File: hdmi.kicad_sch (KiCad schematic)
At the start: 0 parts

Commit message: SCH: Update title block, set revision to 1.0.0
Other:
- company: (none) -> Antmicro Ltd
- title: (none) -> Jetson Orin Baseboard
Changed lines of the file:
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@@
 (kicad_sch (version 20211123) (generator eeschema)
   (paper "A4")
+  (title_block
+    (title "Jetson Orin Baseboard")
+    (rev "1.0.0")
+    (company "Antmicro Ltd")
+    (comment 1 "www.antmicro.com")
+  )
 )

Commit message: Add HDMI connector
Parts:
- added J2: 46756-1001, antmicro-footprints:HDMI_Micro-D_Molex_46765-1x01, symbol antmicroUSBDVIHDMIConnectors:46756-1001
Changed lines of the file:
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@@
     (comment 1 "www.antmicro.com")
   )
+  (symbol (lib_id "antmicroUSBDVIHDMIConnectors:46756-1001") (at 217.17 74.295 0) (unit 1)
+    (in_bom yes) (on_board yes) (fields_autoplaced)
+    (property "Reference" "J2" (id 0) (at 228.092 73.4603 0)
+      (effects (font (size 1.27 1.27)) (justify left))
+    )
+    (property "Value" "46756-1001" (id 1) (at 228.092 75.9972 0)
+      (effects (font (size 1.27 1.27)) (justify left))
+    )
+    (property "Footprint" "antmicro-footprints:HDMI_Micro-D_Molex_46765-1x01" (id 2) (at 217.17 102.235 0)
+      (effects (font (size 1.27 1.27)) hide)
+    )
+    (property "Datasheet" "https://www.molex.com/webdocs/datasheets/pdf/en-us/0467651001_IO_CONNECTORS.pdf" (id 3) (at 217.17 74.295 0)
+      (effects (font (size 1.27 1.27)) hide)
+    )
+    (property "MPN" "467651001" (id 4) (at 217.17 104.775 0)
+      (effects (font (size 1.27 1.27)) hide)
+    )
+    (property "Manufacturer" "Molex" (id 5) (at 217.17 107.315 0)
+      (effects (font (size 1.27 1.27)) hide)
+    )
+    (pin "1")
+    (pin "10")
+    (pin "11")
+    (pin "12")
+    (pin "13")
+    (pin "14")
+    (pin "15")
+    (pin "16")
+    (pin "17")
+    (pin "18")
+    (pin "19")
+    (pin "2")
+    (pin "3")
+    (pin "4")
+    (pin "5")
+    (pin "6")
+    (pin "7")
+    (pin "8")
+    (pin "9")
+    (pin "SH")
+  )
 )

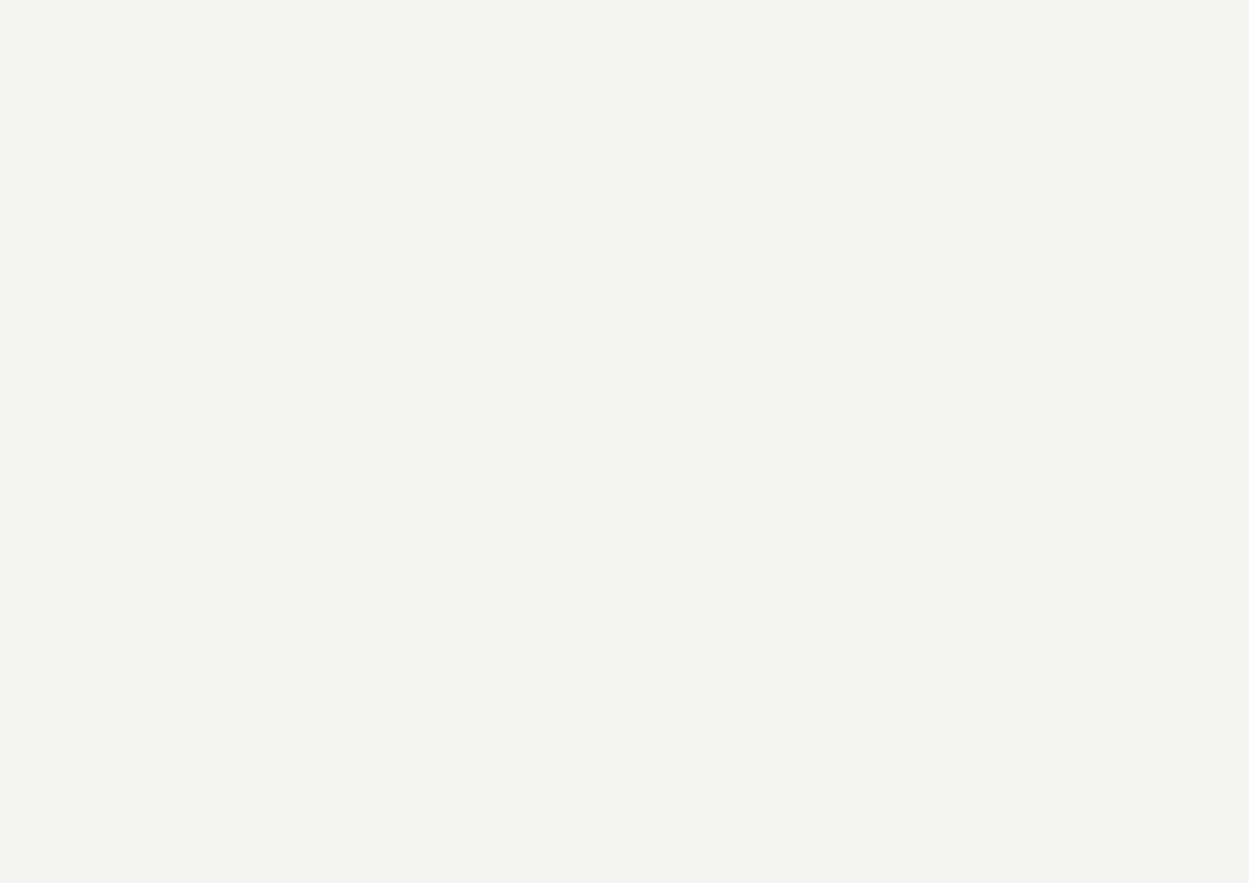
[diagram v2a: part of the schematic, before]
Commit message: Change HDMI/DP net labels, move DP capacitors to HDMI sheet
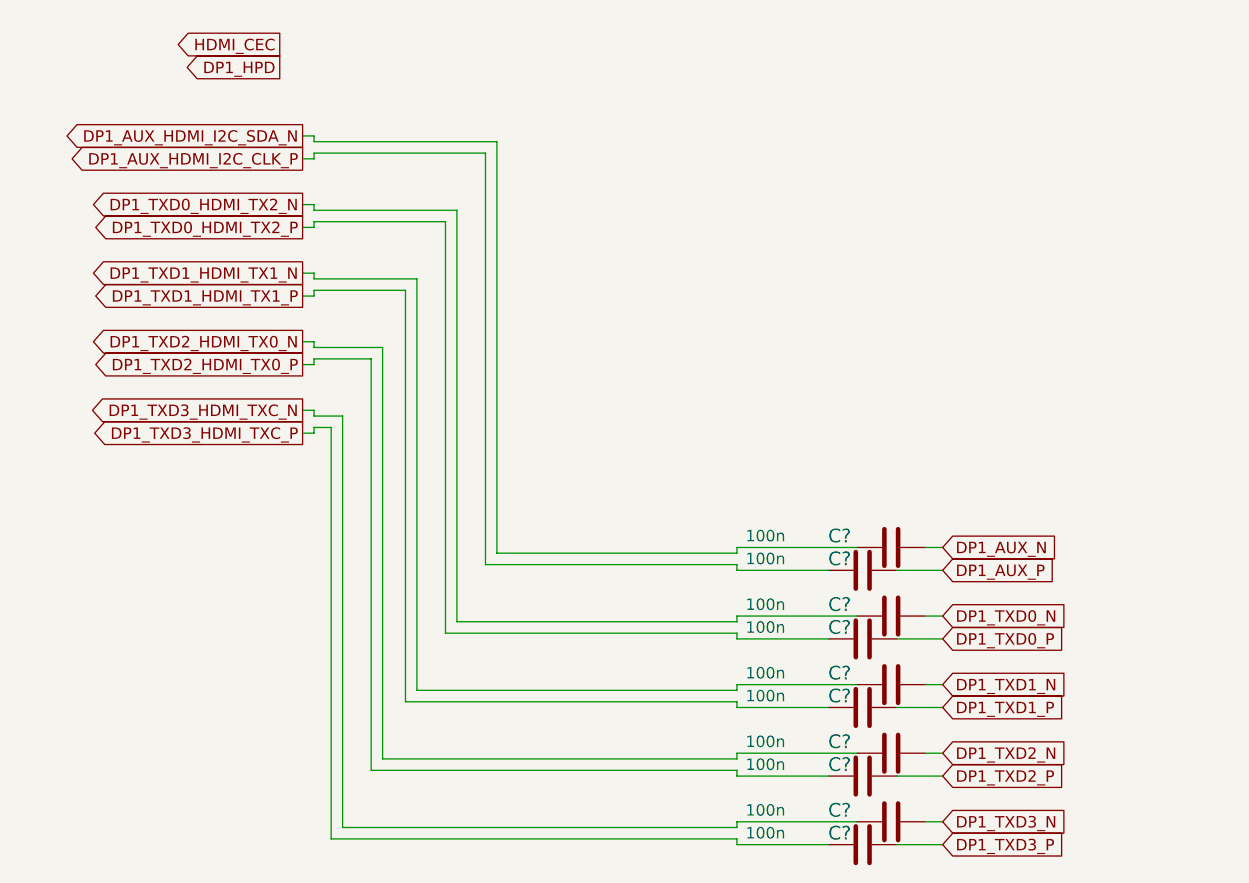
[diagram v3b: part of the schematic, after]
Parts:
- added C? (x10): C_100n_0402, antmicro-footprints:0402-cap, symbol antmicroCapacitors0402:C_100n_0402
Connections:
- new net DP1_AUX_HDMI_I2C_CLK_P: C?.2
- new net DP1_AUX_HDMI_I2C_SDA_N: C?.2
- new net DP1_AUX_N: C?.1
- new net DP1_AUX_P: C?.1
- new net DP1_TXD0_HDMI_TX2_N: C?.2
- new net DP1_TXD0_HDMI_TX2_P: C?.2
- new net DP1_TXD0_N: C?.1
- new net DP1_TXD0_P: C?.1
- new net DP1_TXD1_HDMI_TX1_N: C?.2
- new net DP1_TXD1_HDMI_TX1_P: C?.2
- new net DP1_TXD1_N: C?.1
- new net DP1_TXD1_P: C?.1
- new net DP1_TXD2_HDMI_TX0_N: C?.2
- new net DP1_TXD2_HDMI_TX0_P: C?.2
- new net DP1_TXD2_N: C?.1
- new net DP1_TXD2_P: C?.1
- new net DP1_TXD3_HDMI_TXC_N: C?.2
- new net DP1_TXD3_HDMI_TXC_P: C?.2
- new net DP1_TXD3_N: C?.1
- new net DP1_TXD3_P: C?.1

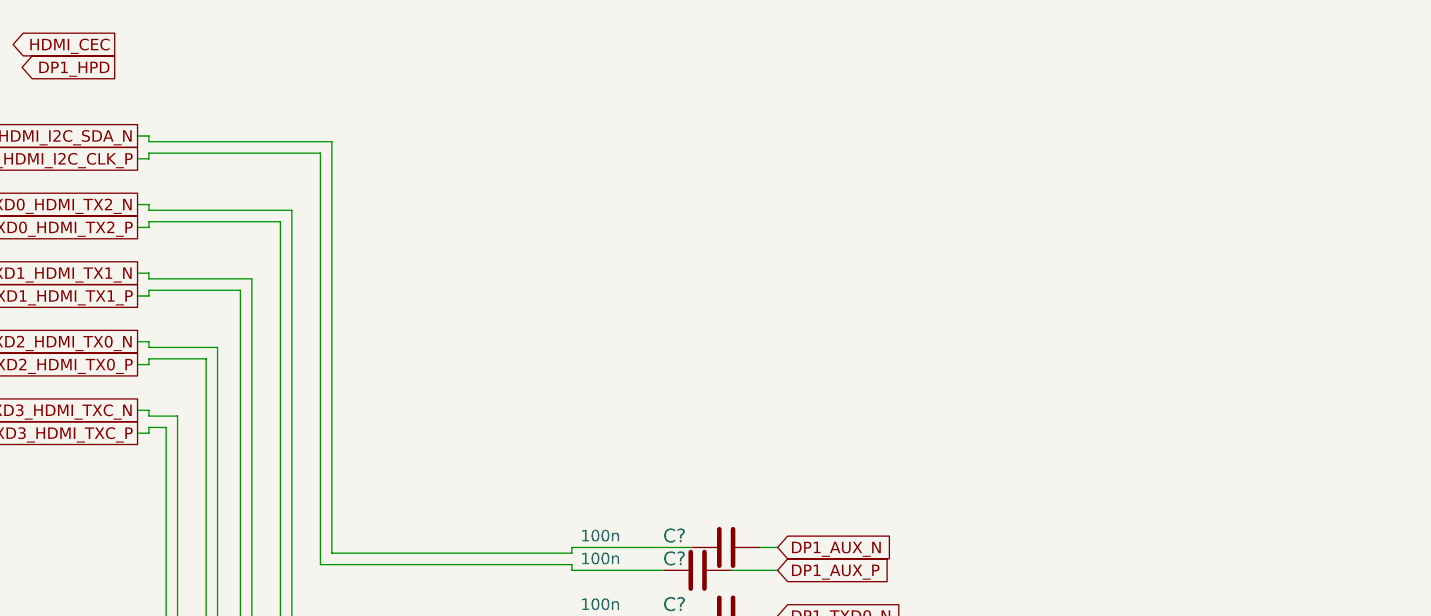
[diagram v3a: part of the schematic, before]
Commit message: Add HDMI AC capacitors
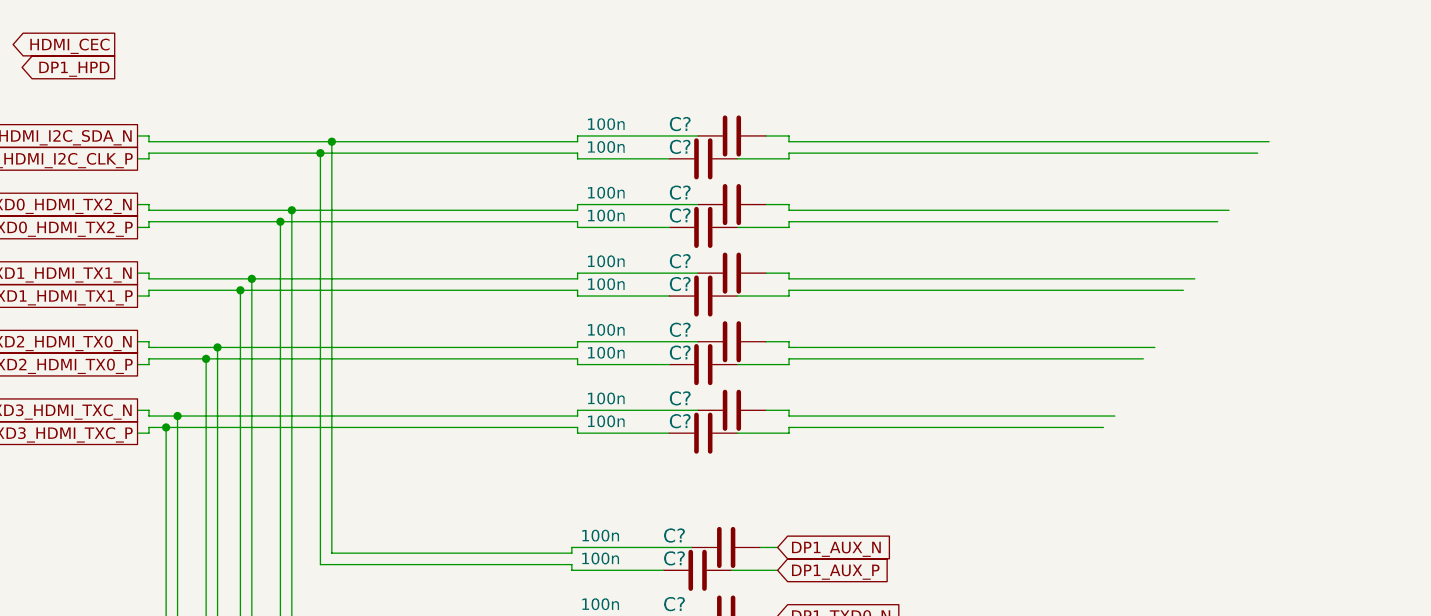
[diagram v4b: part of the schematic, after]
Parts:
- added C? (x10): C_100n_0402, antmicro-footprints:0402-cap, symbol antmicroCapacitors0402:C_100n_0402
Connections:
- net DP1_AUX_HDMI_I2C_CLK_P: now also C?.2
- net DP1_AUX_HDMI_I2C_SDA_N: now also C?.2
- net DP1_TXD0_HDMI_TX2_N: now also C?.2
- net DP1_TXD0_HDMI_TX2_P: now also C?.2
- net DP1_TXD1_HDMI_TX1_N: now also C?.2
- net DP1_TXD1_HDMI_TX1_P: now also C?.2
- net DP1_TXD2_HDMI_TX0_N: now also C?.2
- net DP1_TXD2_HDMI_TX0_P: now also C?.2
- net DP1_TXD3_HDMI_TXC_N: now also C?.2
- net DP1_TXD3_HDMI_TXC_P: now also C?.2

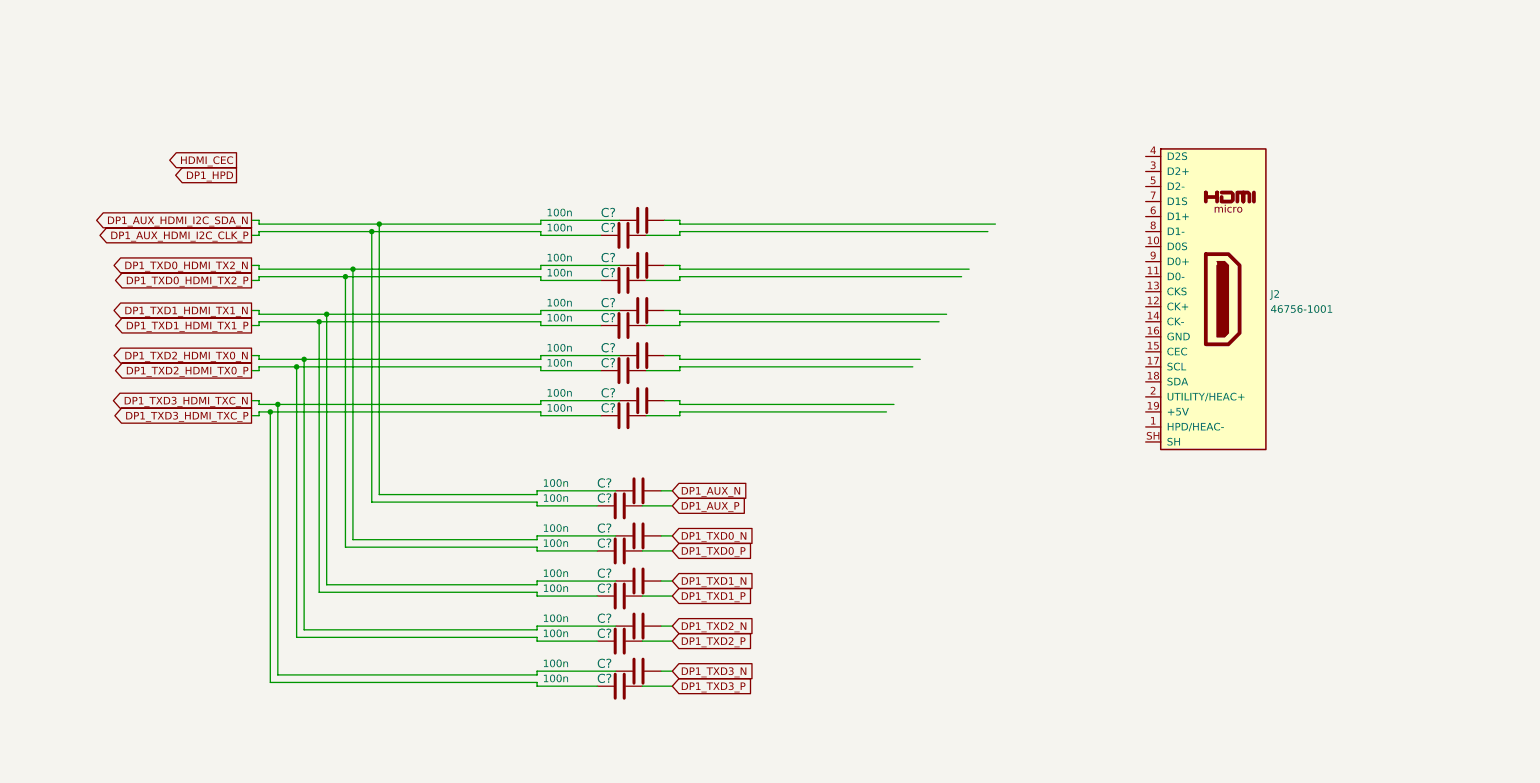
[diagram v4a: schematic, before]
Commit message: Finish HDMI section of the schematics
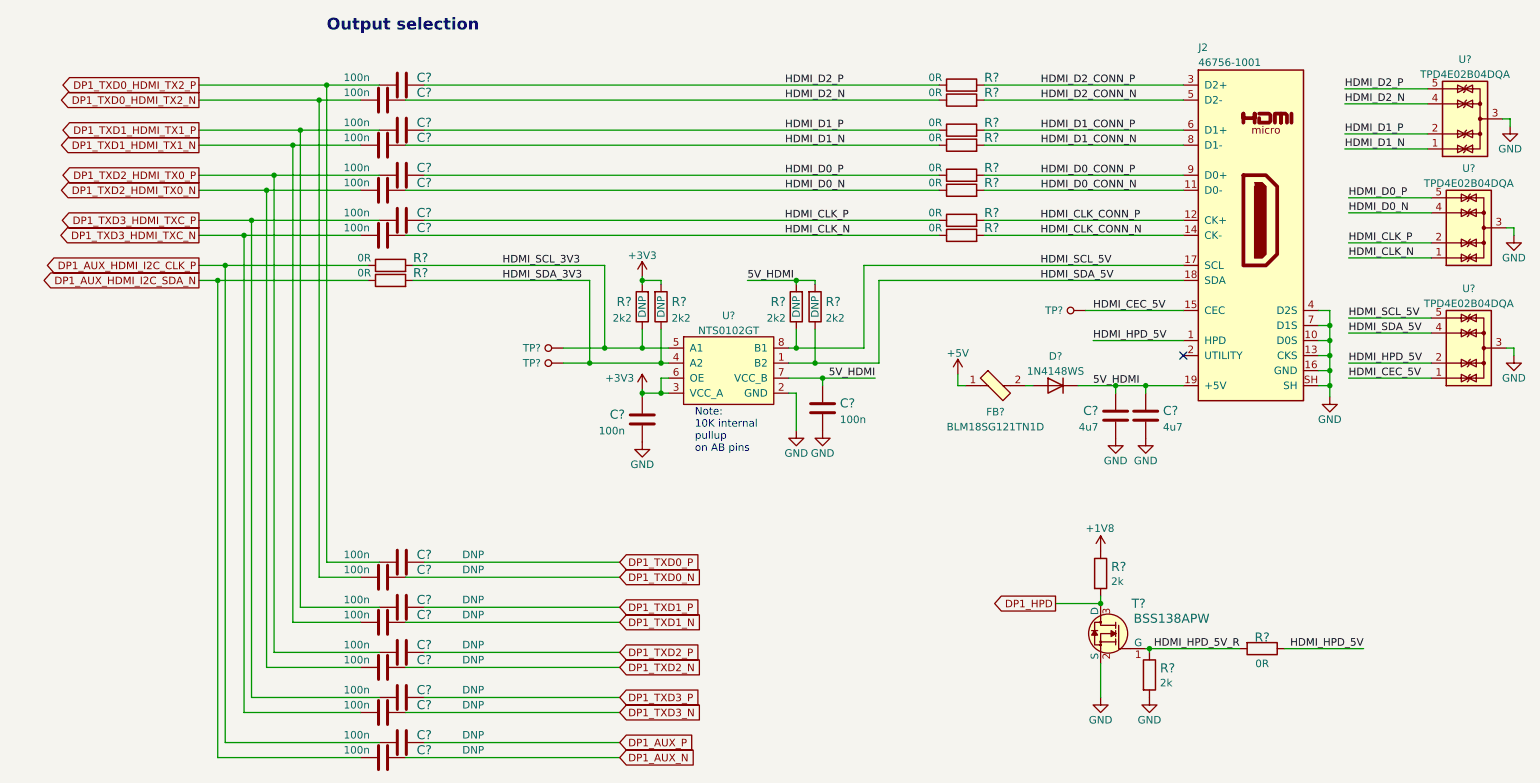
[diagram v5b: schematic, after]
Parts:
- removed C? (x2): C_100n_0402, antmicro-footprints:0402-cap, symbol antmicroCapacitors0402:C_100n_0402
- added C? (x2): C_100n_0402, antmicro-footprints:0402-cap, symbol antmicroCapacitors0402:C_100n_0402
- added C? (x2): C_4u7_0402, antmicro-footprints:0402-cap, symbol antmicroCapacitors0402:C_4u7_0402
- added D?: 1N4148WS, Diode_SMD:D_SOD-323, symbol Diode:1N4148WS
- added FB?: BLM18SG121TN1D, antmicro-footprints:0603-res, symbol antmicroFerriteBeadsandChips:BLM18SG121TN1D
- added R? (x10): R_0R_0402, antmicro-footprints:0402-res, symbol antmicroResistors0402:R_0R_0402
- added R? (x2): R_2k_0402, jetson-nano-baseboard-footprints:0402-res, symbol jetson-nano-baseboard:R_2k_0402
- added R? (x4): R_2k2_0402, antmicro-footprints:0402-res, symbol antmicroResistors0402:R_2k2_0402
- added R?: R_0R_0402, jetson-nano-baseboard-footprints:0402-res, symbol jetson-nano-baseboard:R_0R_0402
- added T?: BSS138APW, jetson-nano-baseboard-footprints:SC70-3, symbol jetson-nano-baseboard:BSS138APW
- added TP? (x3): TP_SMD_0_75MM, antmicro-footprints:Testpoint_smd_0_75mm, symbol antmicroTestPoints:TP_SMD_0_75MM
- added U? (x3): TPD4E02B04DQA, antmicro-footprints:USON-10_2.5x1.0mm_P0.5mm, symbol antmicroTVSDiodes:TPD4E02B04DQA
- added U?: NTS0102GT, antmicro-footprints:PSON50P100X195X50-8N, symbol antmicroLogicTranslatorsLevelShifters:NTS0102GT
- C? (x10): DNP (none) -> DNP
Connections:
- net DP1_AUX_HDMI_I2C_CLK_P: now also C?.2, R?.1; no longer C?.2, C?.2
- net DP1_AUX_HDMI_I2C_SDA_N: now also C?.2, R?.1; no longer C?.2, C?.2
- net DP1_AUX_N: now also C?.1; no longer C?.1
- net DP1_AUX_P: now also C?.1; no longer C?.1
- net DP1_HPD: now also R?.2, T?.3 (D)
- net DP1_TXD0_HDMI_TX2_N: now also C?.2, C?.2; no longer C?.2, C?.2
- net DP1_TXD0_HDMI_TX2_P: now also C?.2, C?.2; no longer C?.2, C?.2
- net DP1_TXD0_N: now also C?.1; no longer C?.1
- net DP1_TXD0_P: now also C?.1; no longer C?.1
- net DP1_TXD1_HDMI_TX1_N: now also C?.2, C?.2; no longer C?.2, C?.2
- net DP1_TXD1_HDMI_TX1_P: now also C?.2, C?.2; no longer C?.2, C?.2
- net DP1_TXD1_N: now also C?.1; no longer C?.1
- net DP1_TXD1_P: now also C?.1; no longer C?.1
- net DP1_TXD2_HDMI_TX0_N: now also C?.2, C?.2; no longer C?.2, C?.2
- net DP1_TXD2_HDMI_TX0_P: now also C?.2, C?.2; no longer C?.2, C?.2
- net DP1_TXD2_N: now also C?.1; no longer C?.1
- net DP1_TXD2_P: now also C?.1; no longer C?.1
- net DP1_TXD3_HDMI_TXC_N: now also C?.2, C?.2; no longer C?.2
- net DP1_TXD3_HDMI_TXC_P: now also C?.2, C?.2; no longer C?.2
- net DP1_TXD3_N: now also C?.1; no longer C?.1
- net DP1_TXD3_P: now also C?.1; no longer C?.1
- net HDMI_HPD_5V: now reaches J2.1 (HPD/HEAC-)
- net HDMI_HPD_5V: now also R?.1, U?.2 (IO2)
- net GND: now reaches J2.10 (D0S)
- net GND: now also J2.13 (CKS), J2.16 (GND), J2.4 (D2S), J2.7 (D1S), J2.SH, C?.1, C?.1, C?.2, C?.2, R?.2, T?.2 (S), U?.2 (GND), U?.3 (G), U?.3 (G), U?.3 (G), U?.8 (G), U?.8 (G), U?.8 (G)
- net HDMI_D0_CONN_N: now reaches J2.11 (D0-)
- net HDMI_D0_CONN_N: now also R?.2
- net HDMI_CLK_CONN_P: now reaches J2.12 (CK+)
- net HDMI_CLK_CONN_P: now also R?.2
- net HDMI_CLK_CONN_N: now reaches J2.14 (CK-)
- net HDMI_CLK_CONN_N: now also R?.2
- net HDMI_CEC_5V: now reaches J2.15 (CEC)
- net HDMI_CEC_5V: now also TP?.1, U?.1 (IO1)
- net HDMI_SCL_5V: now reaches J2.17 (SCL)
- net HDMI_SCL_5V: now also R?.1, U?.5 (IO4), U?.8 (B1)
- net HDMI_SDA_5V: now reaches J2.18 (SDA)
- net HDMI_SDA_5V: now also R?.1, U?.1 (B2), U?.4 (IO3)
- net 5V_HDMI: now reaches J2.19 (+5V)
- net 5V_HDMI: now also C?.1, C?.1, C?.2, D?.1 (K), R?.2, R?.2, U?.7 (VCC_B)
- net HDMI_D2_CONN_P: now reaches J2.3 (D2+)
- net HDMI_D2_CONN_P: now also R?.2
- net HDMI_D2_CONN_N: now reaches J2.5 (D2-)
- net HDMI_D2_CONN_N: now also R?.2
- net HDMI_D1_CONN_P: now reaches J2.6 (D1+)
- net HDMI_D1_CONN_P: now also R?.2
- net HDMI_D1_CONN_N: now reaches J2.8 (D1-)
- net HDMI_D1_CONN_N: now also R?.2
- net HDMI_D0_CONN_P: now reaches J2.9 (D0+)
- net HDMI_D0_CONN_P: now also R?.2
- net HDMI_D1_P: now reaches C?.1
- net HDMI_D1_P: now also R?.1, U?.2 (IO2)
- net HDMI_CLK_P: now reaches C?.1
- net HDMI_CLK_P: now also R?.1, U?.2 (IO2)
- net HDMI_D0_P: now reaches C?.1
- net HDMI_D0_P: now also R?.1, U?.5 (IO4)
- net HDMI_D2_P: now reaches C?.1
- net HDMI_D2_P: now also R?.1, U?.5 (IO4)
- net HDMI_D0_N: now reaches C?.1
- net HDMI_D0_N: now also R?.1, U?.4 (IO3)
- net HDMI_D1_N: now reaches C?.1
- net HDMI_D1_N: now also R?.1, U?.1 (IO1)
- net HDMI_CLK_N: now reaches C?.1
- net HDMI_CLK_N: now also R?.1, U?.1 (IO1)
- net HDMI_D2_N: now reaches C?.1
- net HDMI_D2_N: now also R?.1, U?.4 (IO3)
- new net: D?.2 (A), FB?.2
- new net +1V8: R?.1
- new net +3V3: C?.2, R?.2, R?.2, U?.3 (VCC_A), U?.6 (OE)
- new net +5V: FB?.1
- new net HDMI_HPD_5V_R: R?.1, R?.2, T?.1 (G)
- new net HDMI_SCL_3V3: R?.1, R?.2, TP?.1, U?.5 (A1)
- new net HDMI_SDA_3V3: R?.1, R?.2, TP?.1, U?.4 (A2)
- no-connect marks 0 -> 1
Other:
- note added: "Note: 10K internal pullup on AB pins"
- note added: "Output selection"
- moved on the sheet: C?, J2
